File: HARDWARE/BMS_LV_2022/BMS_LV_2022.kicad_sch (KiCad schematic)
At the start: 33 parts, among them J1 Conn_01x06_Male, J2 Conn_01x12_Male, J3 USB_B_Mini, J4 Battery+, J5 Battery-, SW1 SW_Push, U1 STM32L4P5RET6, Y1 Crystal

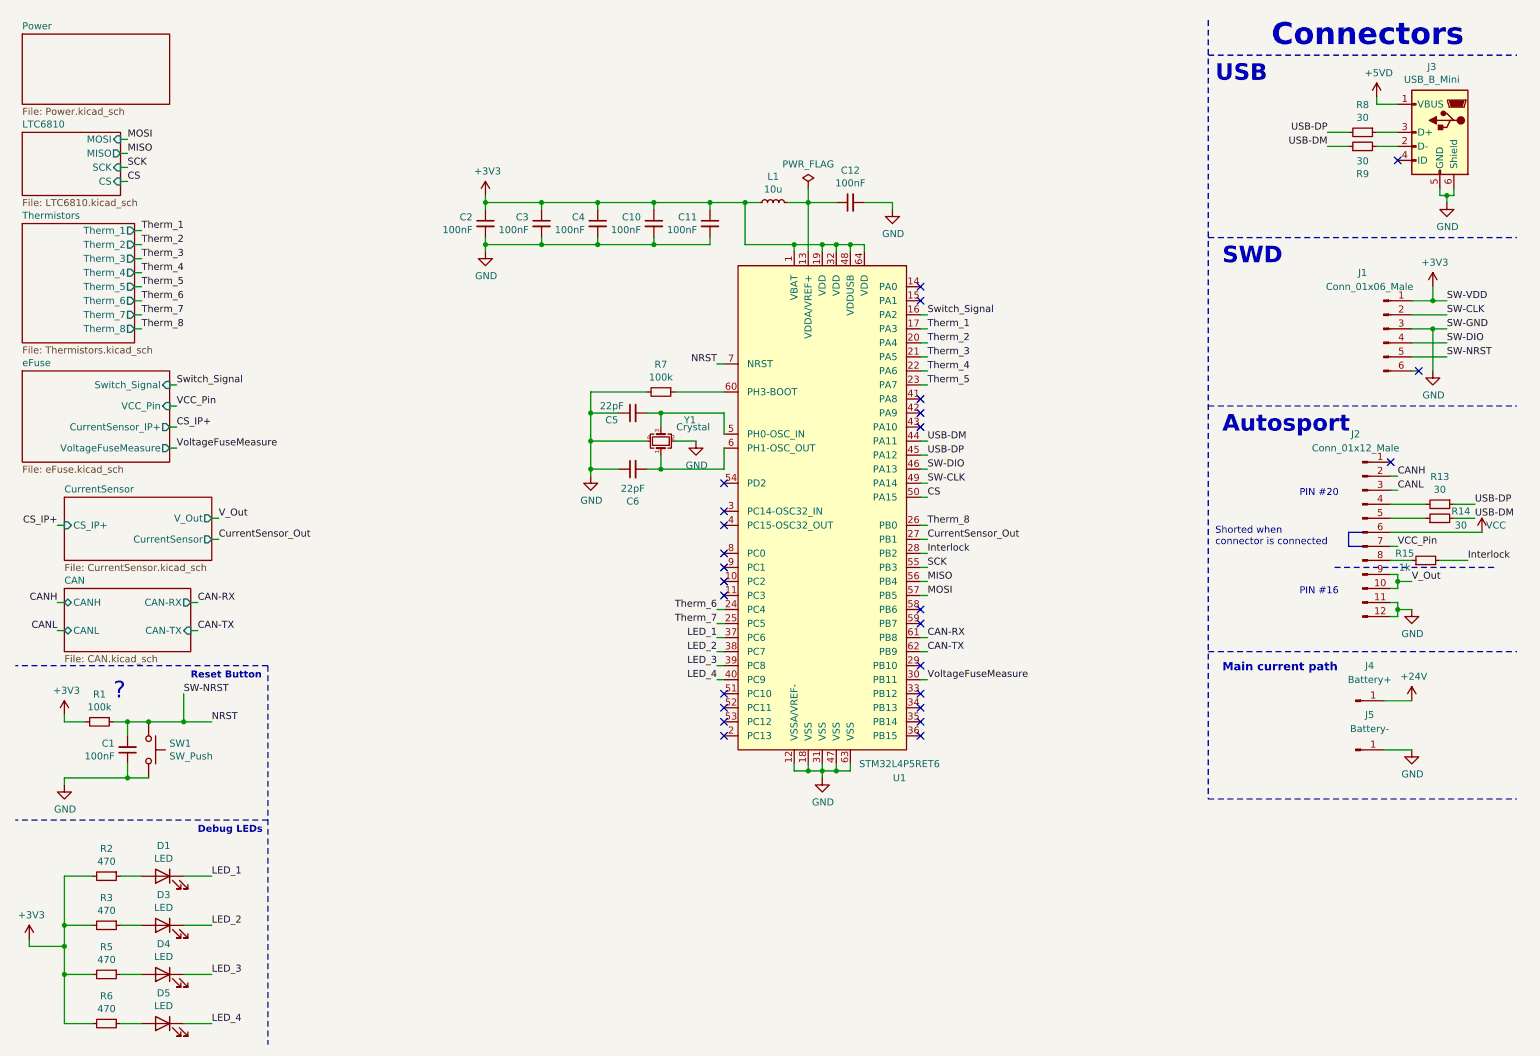
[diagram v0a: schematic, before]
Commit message: New fuses and programming connector added
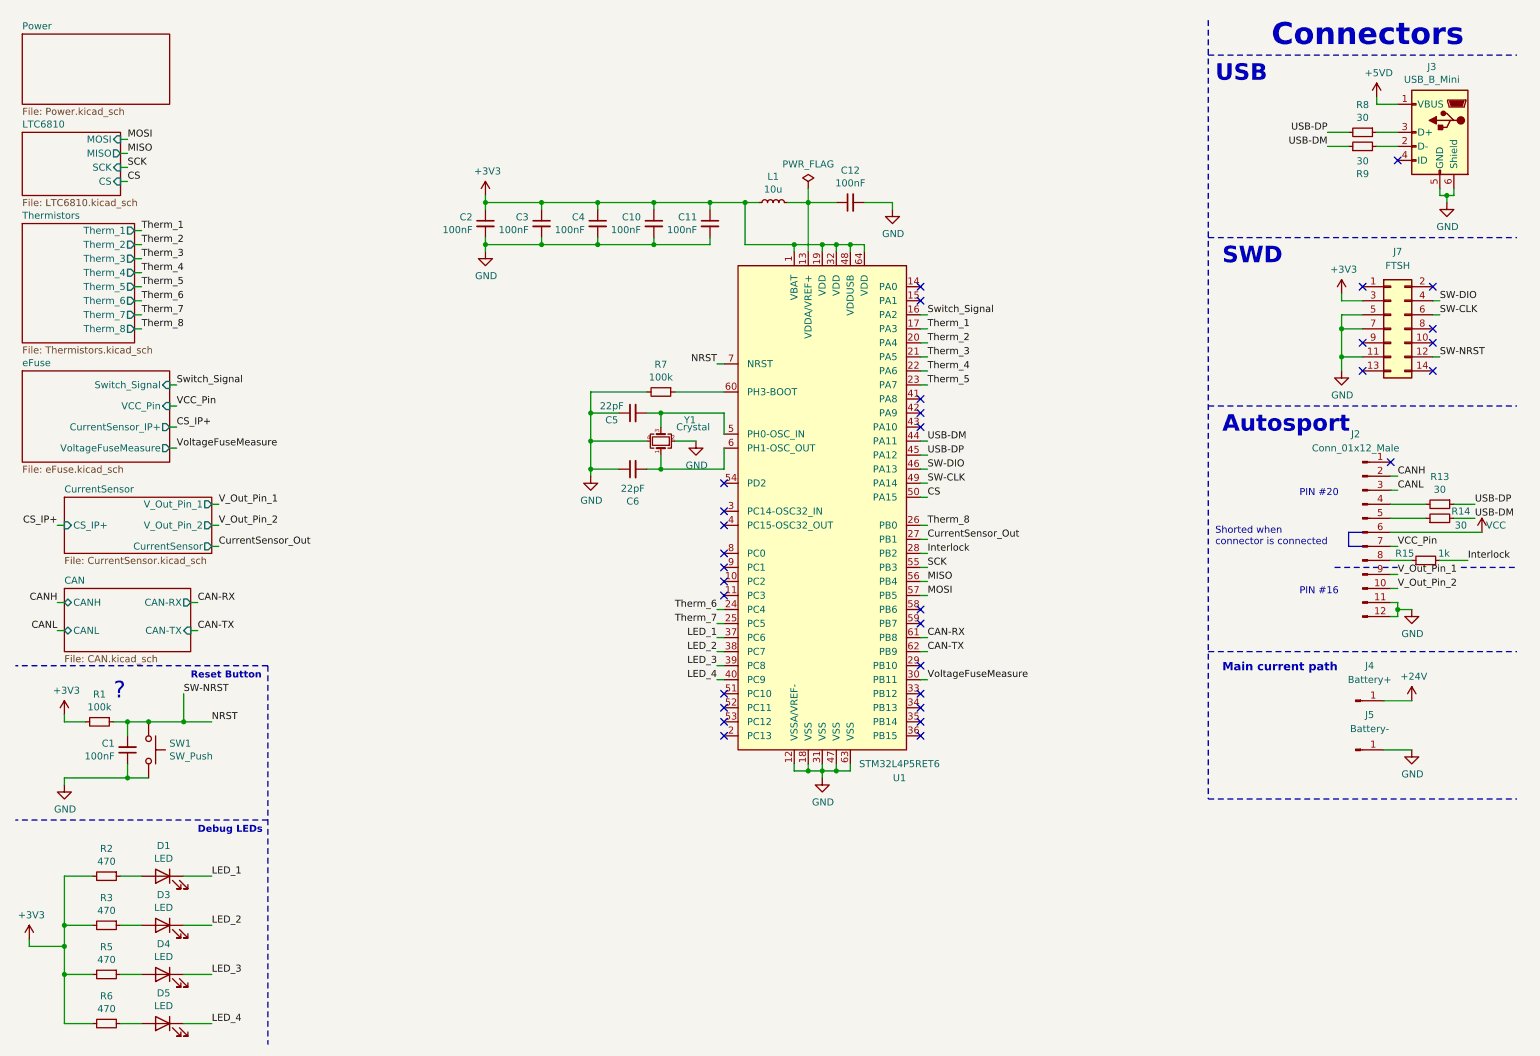
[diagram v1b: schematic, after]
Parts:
- removed J1: Conn_01x06_Male, Connector_PinHeader_2.54mm:PinHeader_1x06_P2.54mm_Vertical, symbol BMS_LV_2022-rescue:Conn_01x06_Male-Connector
- added J7: FTSH, footprints:FTSH-107-XX-YYY-DV-K-A, symbol ftsh-107-01-l-dv-k-a:FTSH-107-01-L-DV-K-A
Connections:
- net +3V3: now also J7.3 (Pin_3)
- net GND: now also J7.11 (Pin_11), J7.5 (Pin_5), J7.7 (Pin_7)
- net NRST: now also J7.12 (Pin_12)
- net SW-CLK: now also J7.6 (Pin_6)
- net SW-DIO: now also J7.4 (Pin_4)
- net V_Out renamed V_Out_Pin_1
- net V_Out_Pin_1: no longer J2.10 (Pin_10)
- new net V_Out_Pin_2: J2.10 (Pin_10)
- no-connect marks 26 -> 32
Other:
- sheet CurrentSensor ports: added V_Out_Pin_1, V_Out_Pin_2; removed V_Out

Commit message: Significant changes
-main connector changed to the other side of the pcb because of using socket connector in the new version
-changed usb mini to usb-c
-changed fuse to 2 fuses protecting current path pins separately
-some minor changes in layout
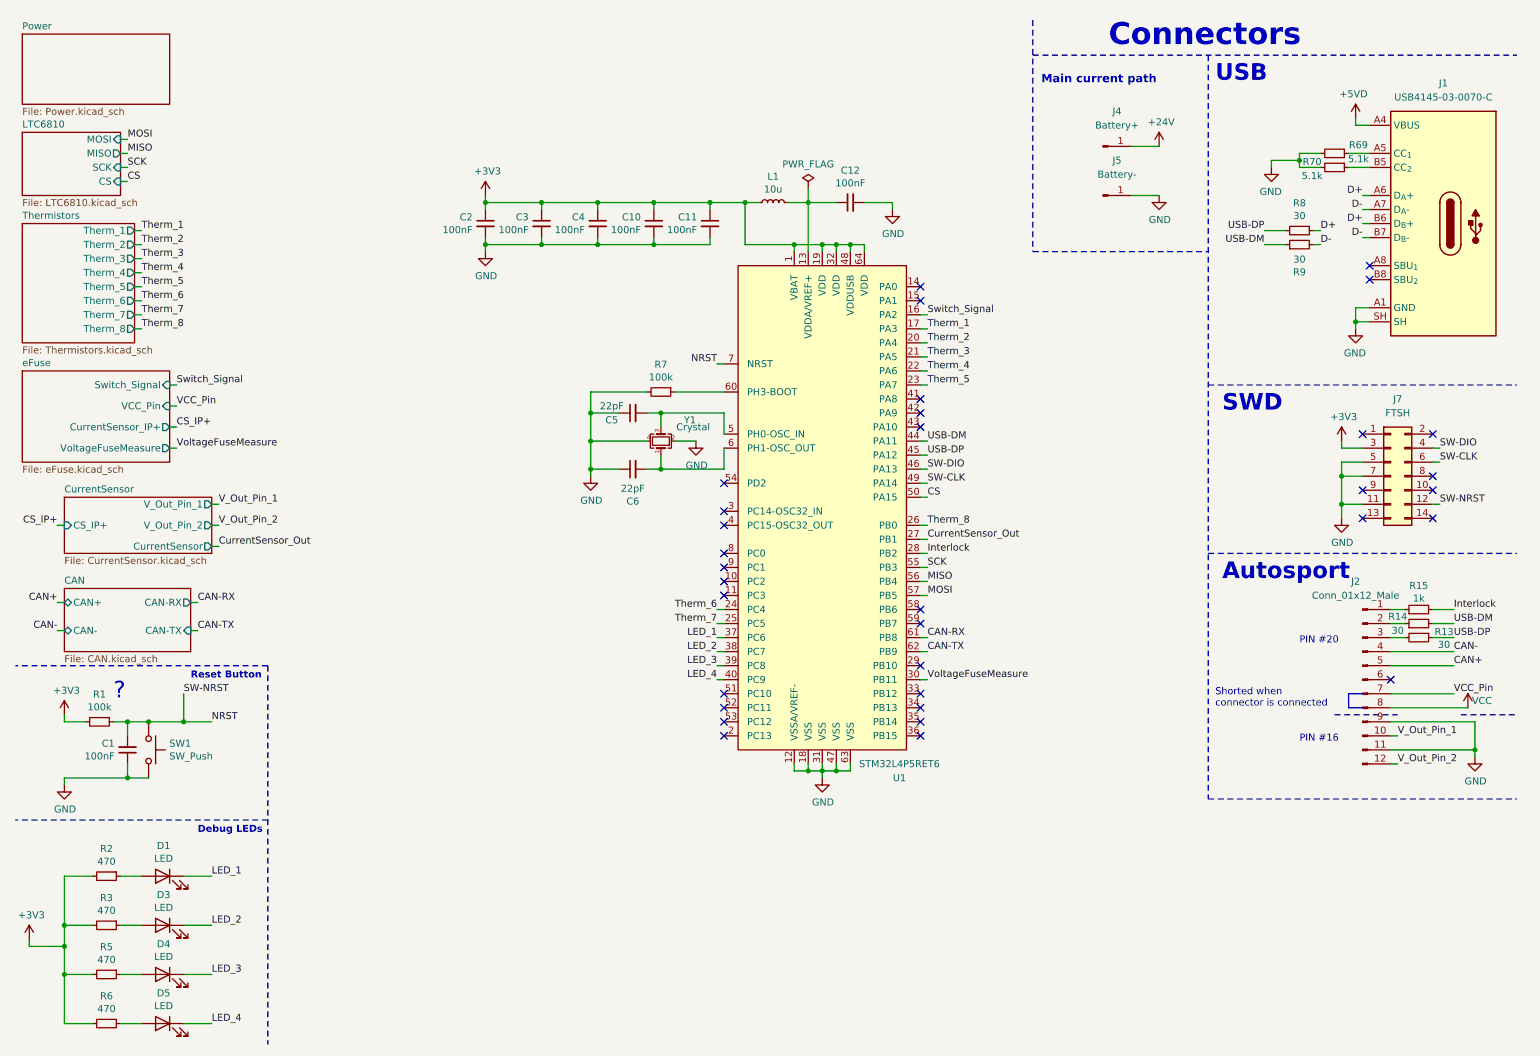
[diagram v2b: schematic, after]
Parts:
- removed J3: USB_B_Mini, Connector_USB:USB_Mini-B_AdamTech_MUSB-B5-S-VT-TSMT-1_SMD_Vertical, symbol BMS_LV_2022-rescue:USB_B_Mini-Connector
- added J1: USB-C_GCT_USB4145-03-0070-C, footprints:USB-C_Receptacle_GCT_USB4145-03-0070-C, symbol USB-C_GCT_USB4145-03-0070-C:USB-C_GCT_USB4145-03-0070-C
- added R69, R70: 5.1k, Resistor_SMD:R_0603_1608Metric, symbol Device:R_Small
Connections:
- net CANH is gone; now on an unnamed net: J2.2 (Pin_2)
- net CANL is gone; now on an unnamed net: J2.3 (Pin_3)
- net +5VD: now also J1.A4 (VBUS), J1.A9 (VBUS), J1.B4 (VBUS), J1.B9 (VBUS)
- net GND: now also J2.9 (Pin_9), J1.A1 (GND), J1.A12 (GND), J1.B1 (GND), J1.B12 (GND), J1.SH, R69.2, R70.2; no longer J2.12 (Pin_12)
- net VCC: now also J2.8 (Pin_8); no longer J2.6 (Pin_6)
- net V_Out_Pin_1: now also J2.10 (Pin_10); no longer J2.9 (Pin_9)
- net V_Out_Pin_2: now also J2.12 (Pin_12); no longer J2.10 (Pin_10)
- net at J2.1 (Pin_1): now also R15.1
- net at R13.2: no longer J2.4 (Pin_4)
- net at R14.1: no longer J2.5 (Pin_5)
- net D-: now reaches R9.2
- net D-: now also J1.A7 (D_{A}-), J1.B7 (D_{B}-)
- net D+: now reaches R8.1
- net D+: now also J1.A6 (D_{A}+), J1.B6 (D_{B}+)
- new net: J1.B5 (CC_{2}), R70.1
- new net: J1.A5 (CC_{1}), R69.1
- new net CAN+: J2.5 (Pin_5)
- new net CAN-: J2.4 (Pin_4)
- no-connect marks 32 -> 33
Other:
- sheet CAN ports: added CAN+, CAN-; removed CANH, CANL
- moved on the sheet: J2, J4, J5, J7, R13, R14, R15, R8, R9
